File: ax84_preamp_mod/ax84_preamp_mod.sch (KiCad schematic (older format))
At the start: 8 parts

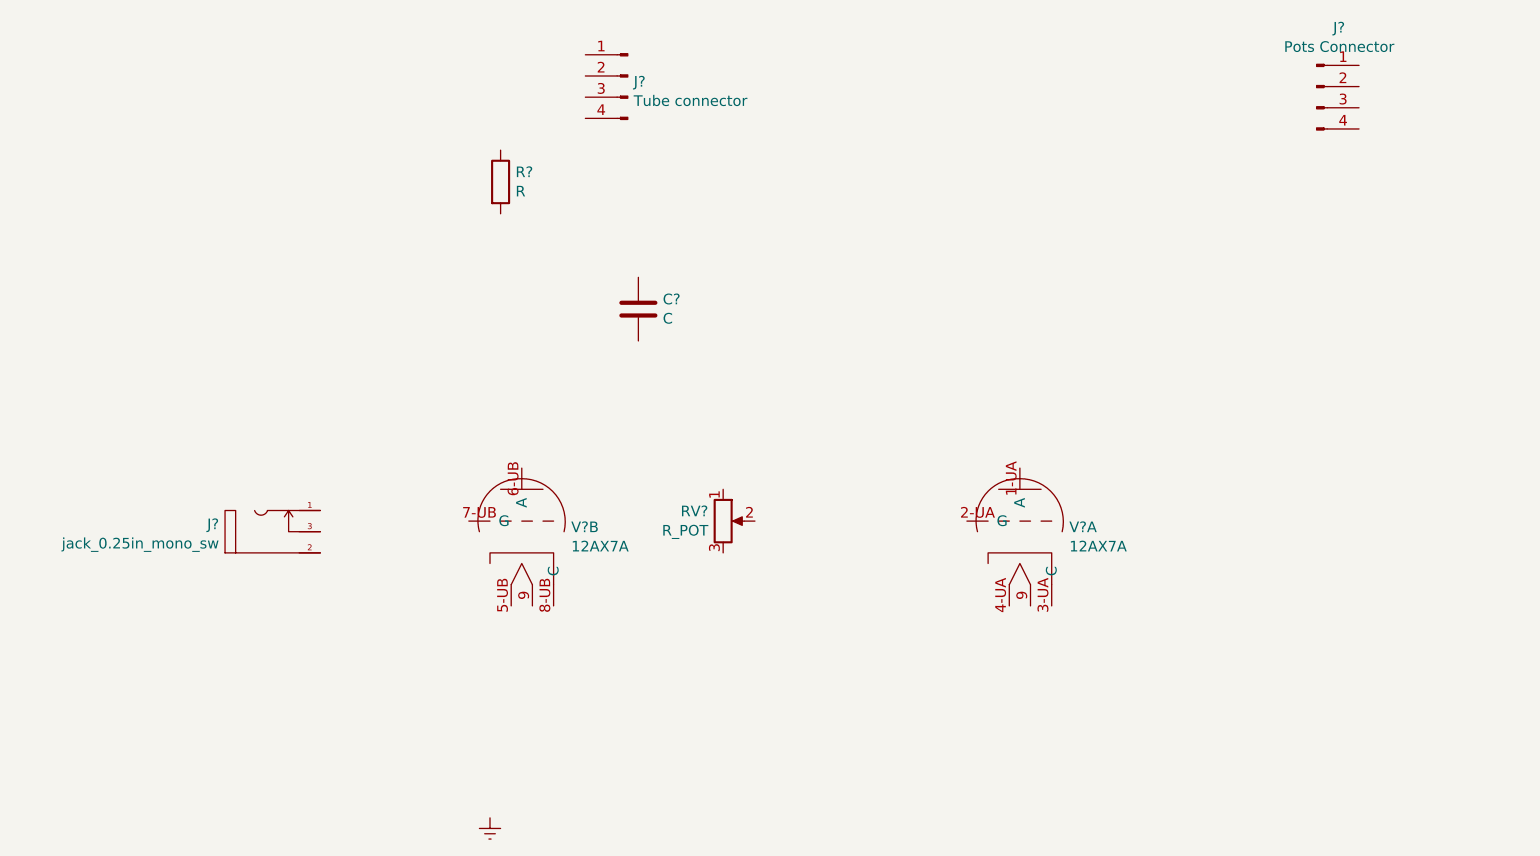
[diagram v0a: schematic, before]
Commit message: schematic and analysis for ax84 preamp mod
Replacing the two separate inputs with a single two stage input to attempt to get nice overdrive tones.
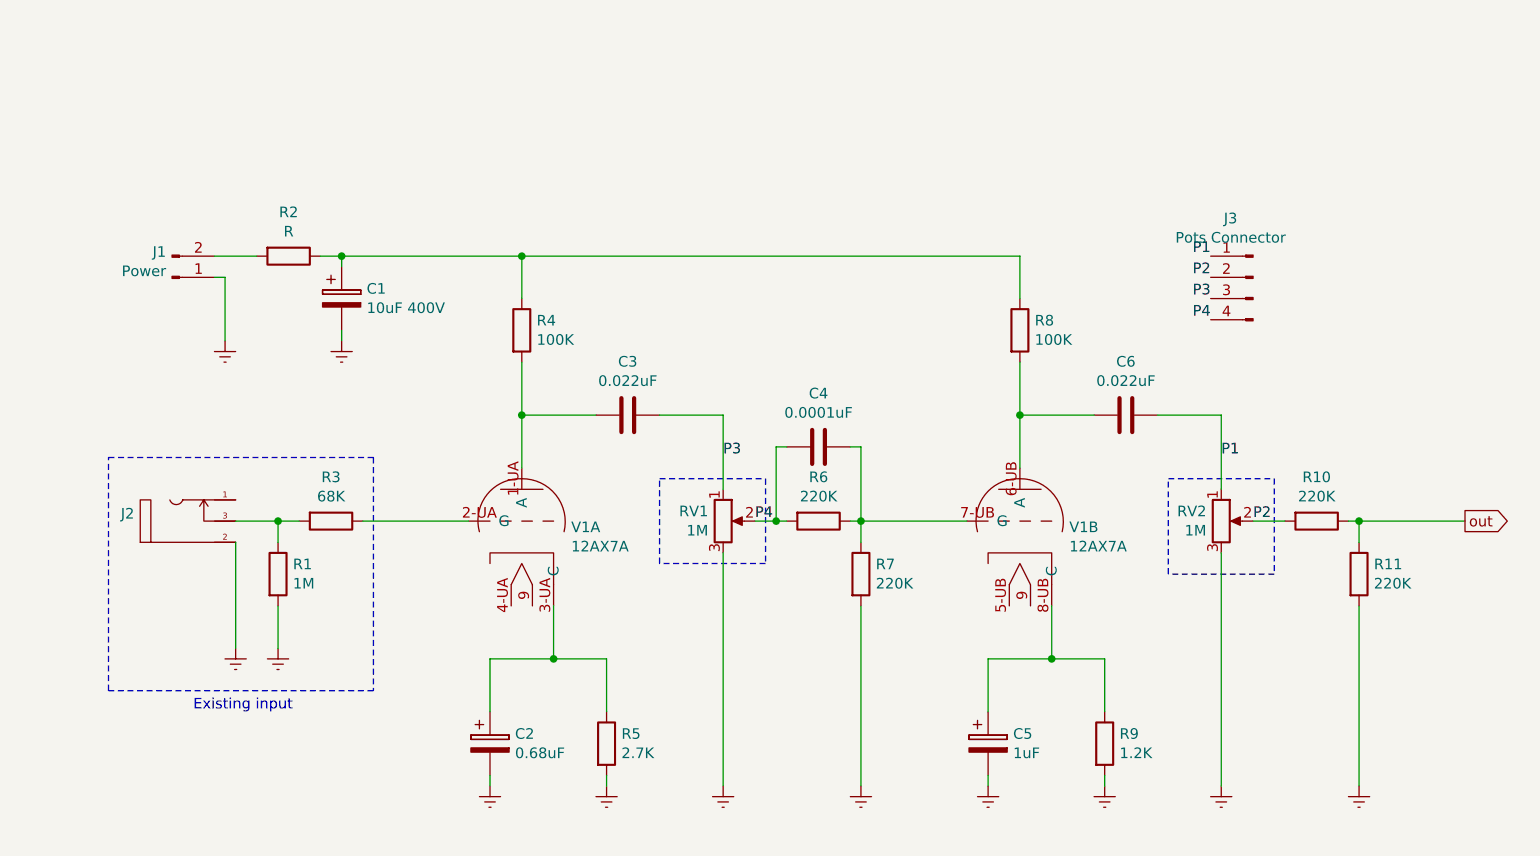
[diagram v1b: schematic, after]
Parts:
- removed C?: C, symbol Device:C
- removed J?: Tube connector, symbol Connector:Conn_01x04_Male
- added C1: 10uF 400V, symbol Device:CP
- added C2: 0.68uF, symbol Device:CP
- added C3, C6: 0.022uF, symbol Device:C
- added C4: 0.0001uF, symbol Device:C
- added C5: 1uF, symbol Device:CP
- added J1: Power, symbol Connector:Conn_01x02_Male
- added R1: 1M, symbol Device:R
- added R10, R11, R6, R7: 220K, symbol Device:R
- added R2: R, symbol Device:R
- added R3: 68K, symbol Device:R
- added R5: 2.7K, symbol Device:R
- added R8: 100K, symbol Device:R
- added R9: 1.2K, symbol Device:R
- added RV2: 1M, symbol Device:R_POT
- R4: renamed from R?; value R -> 100K
- RV1: renamed from RV?; value R_POT -> 1M
- gave numbers to parts that had none: 3
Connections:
- net Earth: now also J2.2, RV1.3, C1.2, C2.2, C5.2, J1.1 (Pin_1), R1.2, R11.2, R5.2, R7.2, R9.2, RV2.3
- net at R4.1: now also C1.1, R2.1, R8.1
- net at R4.2: now also V1.1-UA (A), C3.2
- net at J2.3: now also R1.1, R3.2
- net P1: now reaches J3.1 (Pin_1)
- net P1: now also C6.1, RV2.1
- net P2: now reaches J3.2 (Pin_2)
- net P2: now also R10.2, RV2.2
- net P3: now reaches J3.3 (Pin_3)
- net P3: now also RV1.1, C3.1
- net P4: now reaches J3.4 (Pin_4)
- net P4: now also RV1.2, C4.2, R6.2
- new net: C6.2, R8.2, V1.6-UB (A)
- new net: C4.1, R6.1, R7.1, V1.7-UB (G)
- new net: C5.1, R9.1, V1.8-UB (C)
- new net: R3.1, V1.2-UA (G)
- new net: C2.1, R5.1, V1.3-UA (C)
- new net: J1.2 (Pin_2), R2.2
- new net out: R10.1, R11.1
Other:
- note added: "Existing input"
- moved on the sheet: J2, J3, R4

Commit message: tinkering
remove tone cap. 
update schematic.
combine status with changelog
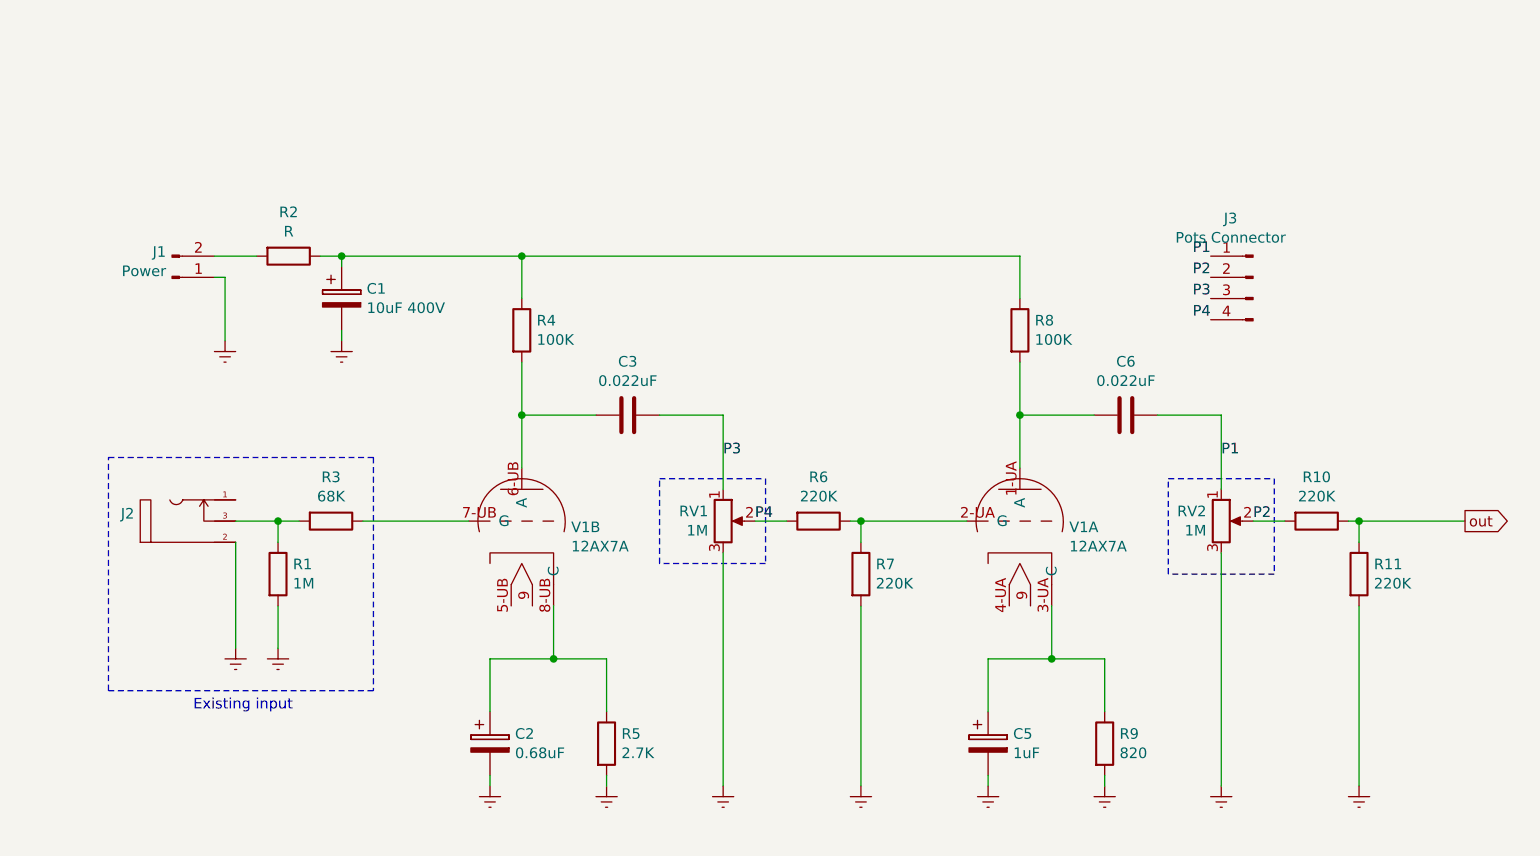
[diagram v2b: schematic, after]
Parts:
- removed C4: 0.0001uF, symbol Device:C
- R9: value 1.2K -> 820
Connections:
- net at C3.2, R4.2: now also V1.6-UB (A); no longer V1.1-UA (A)
- net at C6.2, R8.2: now also V1.1-UA (A); no longer V1.6-UB (A)
- net at R6.1, R7.1: now also V1.2-UA (G); no longer V1.7-UB (G)
- net at C5.1, R9.1: now also V1.3-UA (C); no longer V1.8-UB (C)
- net at R3.1: now also V1.7-UB (G); no longer V1.2-UA (G)
- net at C2.1, R5.1: now also V1.8-UB (C); no longer V1.3-UA (C)
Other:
- moved on the sheet: V1A, V1B
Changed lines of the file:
@@
 L yga1:12AX7A V1
 U 2 1 5C649C69
+P 2750 3450
+F 0 "V1" H 2983 3671 50  0000 L CNN
+F 1 "12AX7A" H 2983 3580 50  0000 L CNN
+F 2 "" H 2750 3100 50  0001 C CNN
+F 3 "" H 2750 3100 50  0001 C CNN
+	2    2750 3450
+	1    0    0    -1
+$EndComp
+$Comp
+L yga1:12AX7A V1
+U 1 1 5C649D19
 P 5100 3450
 F 0 "V1" H 5333 3671 50  0000 L CNN
@@
 F 2 "" H 5100 3100 50  0001 C CNN
 F 3 "" H 5100 3100 50  0001 C CNN
-	2    5100 3450
-	1    0    0    -1
-$EndComp
-$Comp
-L yga1:12AX7A V1
-U 1 1 5C649D19
-P 2750 3450
-F 0 "V1" H 2983 3671 50  0000 L CNN
-F 1 "12AX7A" H 2983 3580 50  0000 L CNN
-F 2 "" H 2750 3100 50  0001 C CNN
-F 3 "" H 2750 3100 50  0001 C CNN
-	1    2750 3450
+	1    5100 3450
 	1    0    0    -1
 $EndComp
@@
 	0    1    1    0
 $EndComp
-$Comp
-L Device:C C4
-U 1 1 5C75A67F
-P 4150 2850
-F 0 "C4" V 3898 2850 50  0000 C CNN
-F 1 "0.0001uF" V 3989 2850 50  0000 C CNN
-F 2 "" H 4188 2700 50  0001 C CNN
-F 3 "~" H 4150 2850 50  0001 C CNN
-	1    4150 2850
-	0    1    1    0
-$EndComp
-Wire Wire Line
-	4000 2850 3950 2850
-Wire Wire Line
-	3950 2850 3950 3200
-Wire Wire Line
-	3950 3200 3850 3200
-Wire Wire Line
-	4000 3200 3950 3200
-Connection ~ 3950 3200
 Wire Wire Line
 	4300 3200 4350 3200
-Wire Wire Line
-	4350 3200 4350 2850
-Wire Wire Line
-	4350 2850 4300 2850
 $Comp
 L Device:R R7
@@
 P 5500 4250
 F 0 "R9" H 5570 4296 50  0000 L CNN
-F 1 "1.2K" H 5570 4205 50  0000 L CNN
+F 1 "820" H 5570 4205 50  0000 L CNN
 F 2 "" V 5430 4250 50  0001 C CNN
 F 3 "~" H 5500 4250 50  0001 C CNN
@@
 Text Label 6000 2250 2    50   ~ 0
 P4
+Wire Wire Line
+	3850 3200 4000 3200
 $EndSCHEMATC
